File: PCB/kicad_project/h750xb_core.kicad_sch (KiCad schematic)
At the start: 3 parts

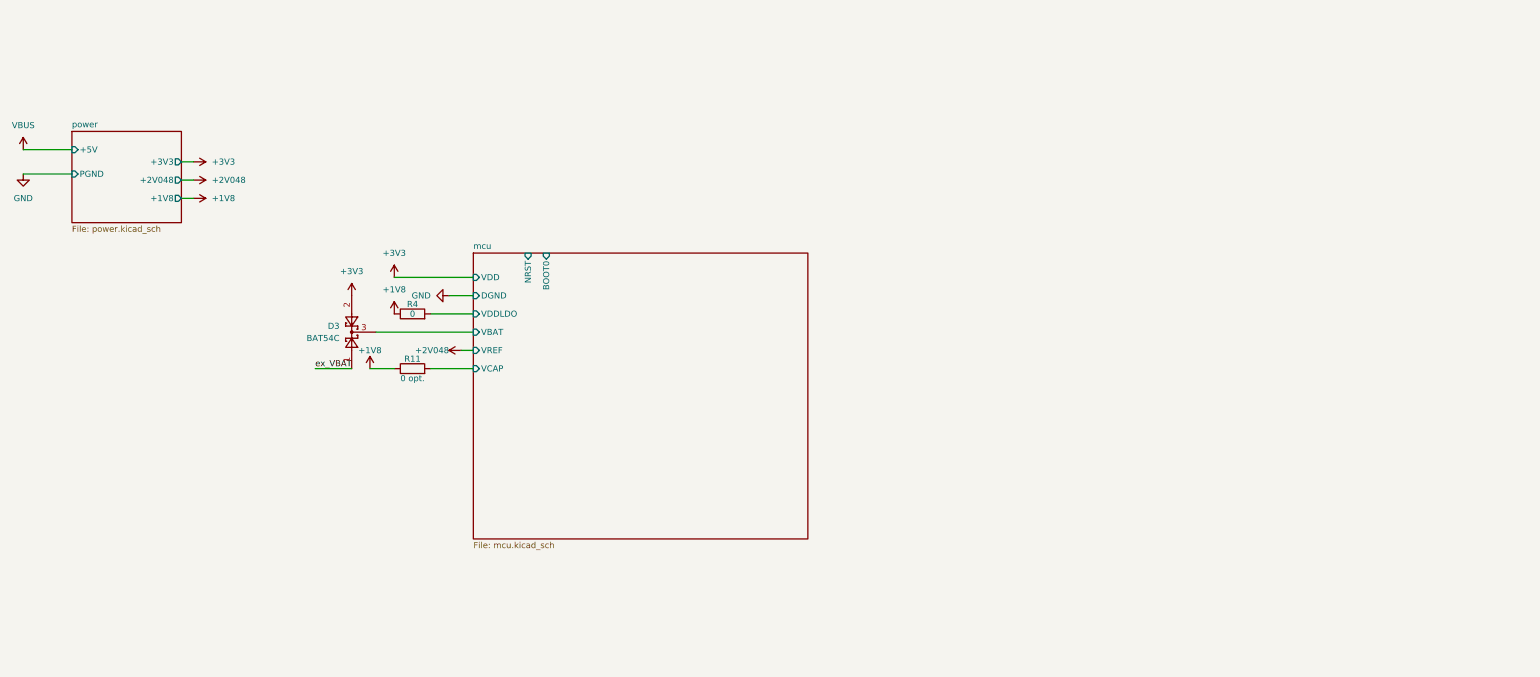
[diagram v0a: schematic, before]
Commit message: 更新原理图网络和PCB部分IO走线
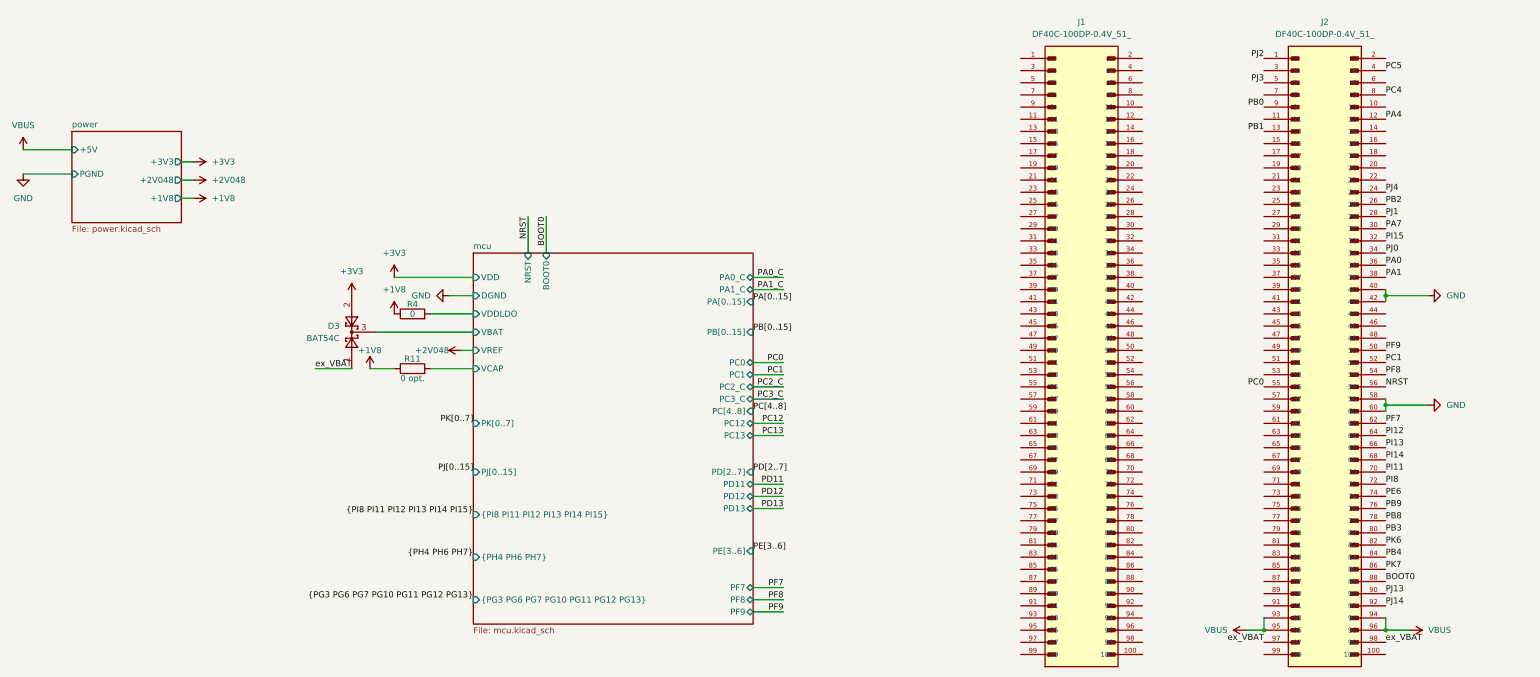
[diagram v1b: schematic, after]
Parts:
- added J1, J2: DF40C-100DP-0.4V_51_, HRS:HIROSE_DF40C-100DP-0.4V_51_, symbol DF40C-100DP-0.4V_51_:DF40C-100DP-0.4V_51_
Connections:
- net GND: now also J2.40, J2.42, J2.58, J2.60
- net VBUS: now also J2.93, J2.94, J2.95, J2.96
- net ex_VBAT: now also J2.97, J2.98
- new net BOOT0: J2.88
- new net NRST: J2.56
- new net PA0: J2.36
- new net PA1: J2.38
- new net PA4: J2.12
- new net PA7: J2.30
- new net PB0: J2.9
- new net PB1: J2.13
- new net PB2: J2.26
- new net PB3: J2.80
- new net PB4: J2.84
- new net PB8: J2.78
- new net PB9: J2.76
- new net PC0: J2.55
- new net PC1: J2.52
- new net PC4: J2.8
- new net PC5: J2.4
- new net PE6: J2.74
- new net PF7: J2.62
- new net PF8: J2.54
- new net PF9: J2.50
- new net PI11: J2.70
- new net PI12: J2.64
- new net PI13: J2.66
- new net PI14: J2.68
- new net PI15: J2.32
- new net PI8: J2.72
- new net PJ0: J2.34
- new net PJ1: J2.28
- new net PJ13: J2.90
- new net PJ14: J2.92
- new net PJ2: J2.1
- new net PJ3: J2.5
- new net PJ4: J2.24
- new net PK6: J2.82
- new net PK7: J2.86
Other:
- sheet mcu ports: added PA0_C, PA1_C, PA[0..15], PB[0..15], PC0, PC1, PC12, PC13, PC2_C, PC3_C, PC[4..8], PD11, PD12, PD13, PD[2..7], PE[3..6], PF7, PF8, PF9, PJ[0..15], PK[0..7], {PG3 PG6 PG7 PG10 PG11 PG12 PG13}, {PH4 PH6 PH7}, {PI8 PI11 PI12 PI13 PI14 PI15}; removed none

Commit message: 完工0-0
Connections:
- net PC4 is gone; now on net GND: J2.8
- net ex_VBAT is gone; now on net GND: D3.1, J2.97, J2.98
- net +3V3: now also J2.39, J2.41, J2.43, J2.45, J2.47, J2.49
- net GND: now also J1.1, J1.100, J1.12, J1.13, J1.16, J1.17, J1.2, J1.21, J1.22, J1.25, J1.26, J1.29, J1.30, J1.33, J1.34, J1.37, J1.38, J1.4, J1.41, J1.42, J1.45, J1.46, J1.49, J1.5, J1.50, J1.53, J1.54, J1.57, J1.58, J1.6, J1.61, J1.62, J1.65, J1.66, J1.69, J1.70, J1.73, J1.74, J1.77, J1.78, J1.8, J1.81, J1.82, J1.85, J1.86, J1.89, J1.9, J1.90, J1.93, J1.94, J1.97, J1.98, J1.99, J2.10, J2.100, J2.11, J2.14, J2.15, J2.16, J2.18, J2.2, J2.20, J2.22, J2.23, J2.3, J2.37, J2.44, J2.46, J2.48, J2.51, J2.53, J2.6, J2.7, J2.73, J2.77, J2.81, J2.85, J2.87, J2.89, J2.91, J2.99
- net PA0_C: now also J2.25
- net PA1_C: now also J2.21
- net PC12: now also J1.43
- net PC13: now also J2.57
- net PC2_C: now also J2.31
- net PC3_C: now also J2.29
- net PD11: now also J1.92
- net PD12: now also J1.95
- net PD13: now also J1.91
- net PD2: now reaches J1.10
- net PG11: now reaches J1.11
- net PA13: now reaches J1.14
- net PJ15: now reaches J1.15
- net PA12: now reaches J1.18
- net PD7: now reaches J1.19
- net PA11: now reaches J1.20
- net PD6: now reaches J1.23
- net PA10: now reaches J1.24
- net PD5: now reaches J1.27
- net PA9: now reaches J1.28
- net PG12: now reaches J1.3
- net PJ12: now reaches J1.31
- net PA8: now reaches J1.32
- net PD3: now reaches J1.35
- net PC8: now reaches J1.36
- net PD4: now reaches J1.39
- net PG7: now reaches J1.40
- net PK0: now reaches J1.44
- net PA15: now reaches J1.47
- net PJ11: now reaches J1.48
- net PA14: now reaches J1.51
- net PB11: now reaches J1.52
- net PC7: now reaches J1.55
- net PJ8: now reaches J1.56
- net PC6: now reaches J1.59
- net PJ7: now reaches J1.60
- net PK2: now reaches J1.63
- net PB10: now reaches J1.64
- net PG6: now reaches J1.67
- net PJ5: now reaches J1.68
- net PG10: now reaches J1.7
- net PG3: now reaches J1.71
- net PH7: now reaches J1.72
- net PK1: now reaches J1.75
- net PB13: now reaches J1.76
- net PJ10: now reaches J1.79
- net PB12: now reaches J1.80
- net PJ9: now reaches J1.83
- net PB14: now reaches J1.84
- net PJ6: now reaches J1.87
- net PB15: now reaches J1.88
- net PH6: now reaches J1.96
- net PA5: now reaches J2.17
- net PA3: now reaches J2.19
- net PA6: now reaches J2.27
- net PH4: now reaches J2.33
- net PA2: now reaches J2.35
- net PE5: now reaches J2.59
- net PE4: now reaches J2.61
- net PE3: now reaches J2.63
- net PB7: now reaches J2.65
- net PB6: now reaches J2.67
- net PB5: now reaches J2.69
- net PK3: now reaches J2.71
- net PK4: now reaches J2.75
- net PK5: now reaches J2.79
- net PG13: now reaches J2.83
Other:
- moved on the sheet: J2
